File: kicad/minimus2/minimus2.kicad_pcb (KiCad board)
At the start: 2 copper layers, 69 x 38 mm, 84 parts, among them J1 PROG_SER, J2 LM, J3 LM, Q1 SSM6N58NU_LF, Q2 SSM6N58NU_LF, Q3 DMN3051L, SW1 RESET, SW2 USER_A, SW4 SW_SPDT, U1 LSM6DSRTR, U2 STM32U575CITx, U3 DRV8835, U4 AS5047D, U5 AS5047D, U6 AP2210N-3.3TRG1, U9 AP7370-50FDC

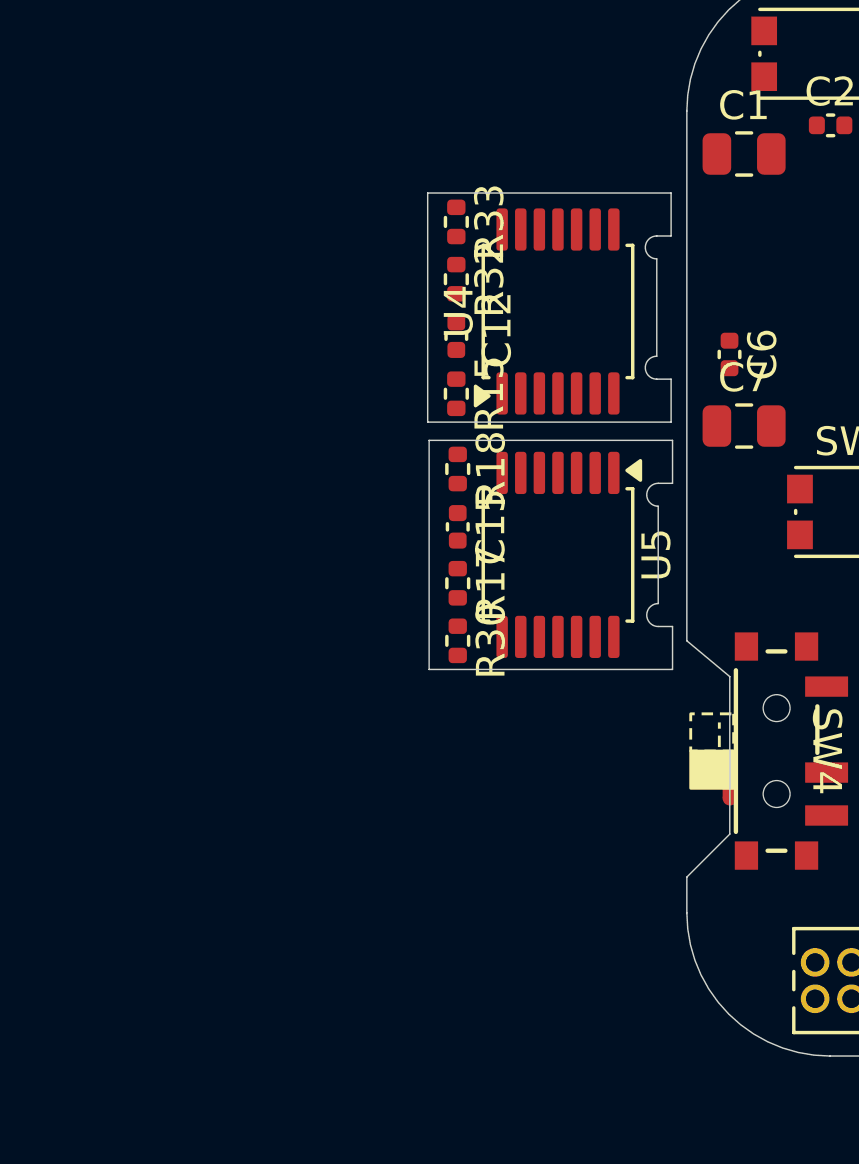
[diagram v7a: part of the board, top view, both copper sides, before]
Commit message: update encoder board size
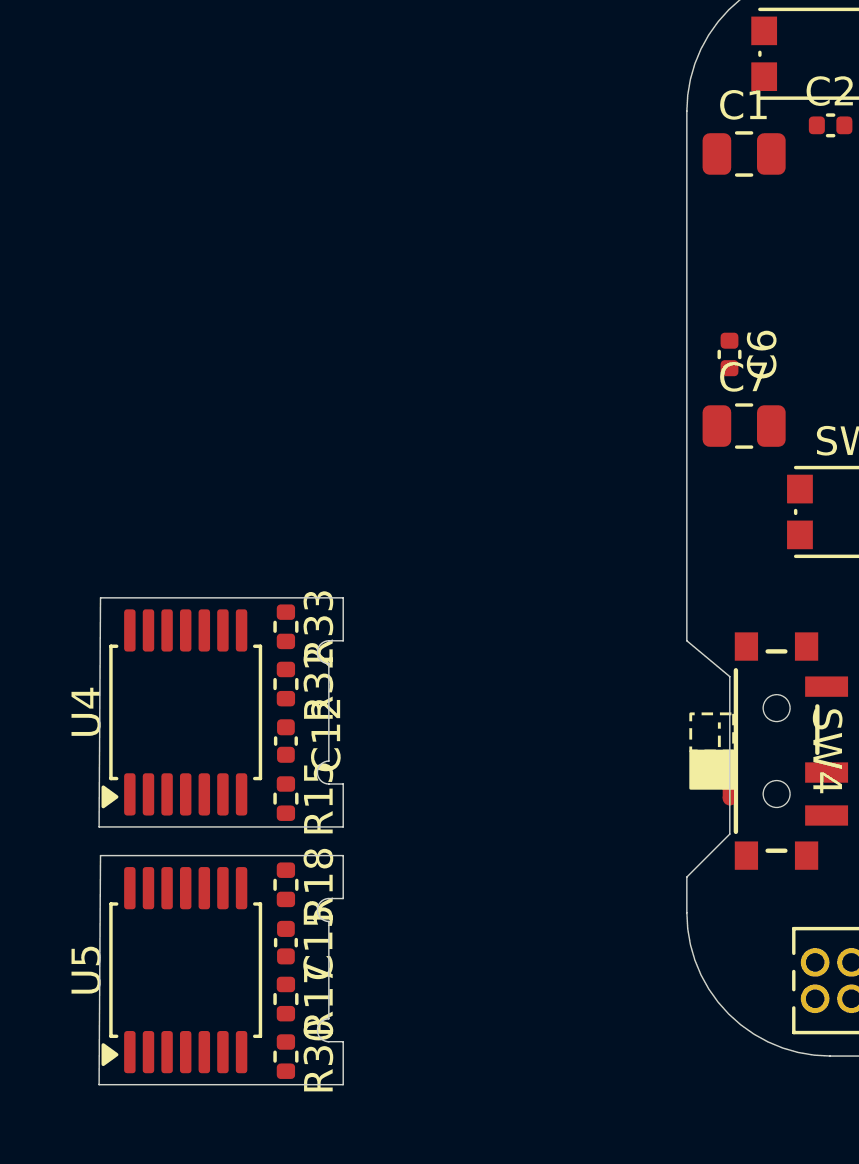
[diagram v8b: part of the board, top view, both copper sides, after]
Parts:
- moved U5 19.5 mm to (57.5, 116.0), turned to 90 degrees
- moved U4 19.1 mm to (57.5, 107.0)
- moved C15 15.7 mm to (61.0, 115.0)
- moved R17 15.7 mm to (61.0, 117.0)
- moved R18 15.7 mm to (61.0, 113.0)
- moved R30 15.7 mm to (61.0, 119.0)
- moved C12 15.3 mm to (61.0, 108.0)
- moved R15 15.3 mm to (61.0, 110.0)
- moved R32 15.3 mm to (61.0, 106.0)
- moved R33 15.3 mm to (61.0, 104.0)
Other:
- board size 69 x 38 mm -> 80.5 x 39 mm
